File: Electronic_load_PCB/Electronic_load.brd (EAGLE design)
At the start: 121.9 x 88.6 mm, 111 parts, among them IC7 LM1117IMPX-5.0, J1 XT60-M, J2 B2B-XH, J3 B4B-XH, J4 B2B-XH, J5 B2B-XH, J6 B2B-XH, J7 B2B-XH, J8 B5B-XH, Q1 IRFP250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

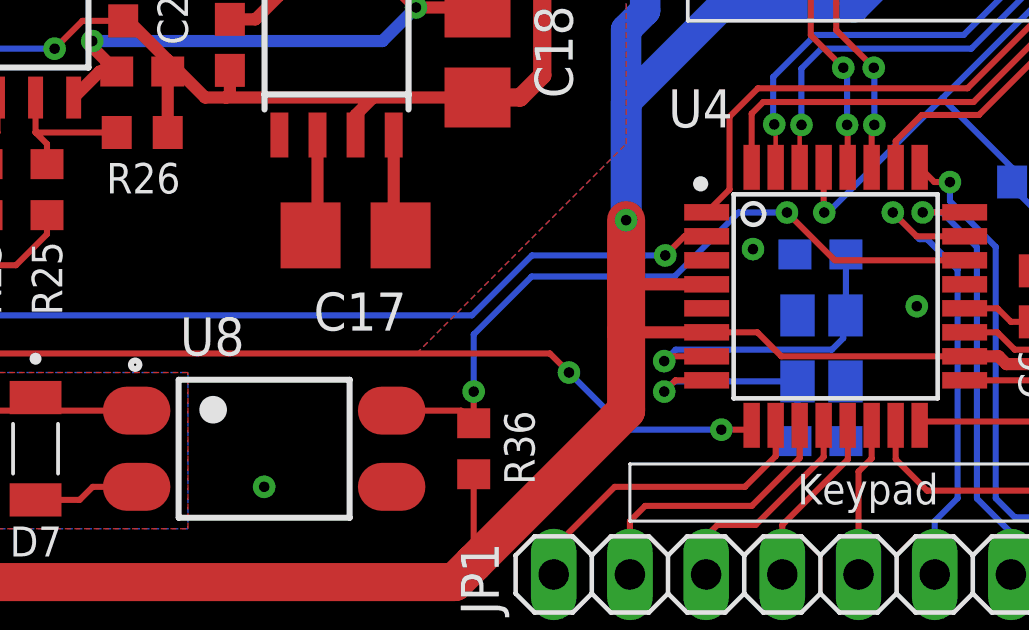
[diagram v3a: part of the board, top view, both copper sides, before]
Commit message: cleaned up schematic
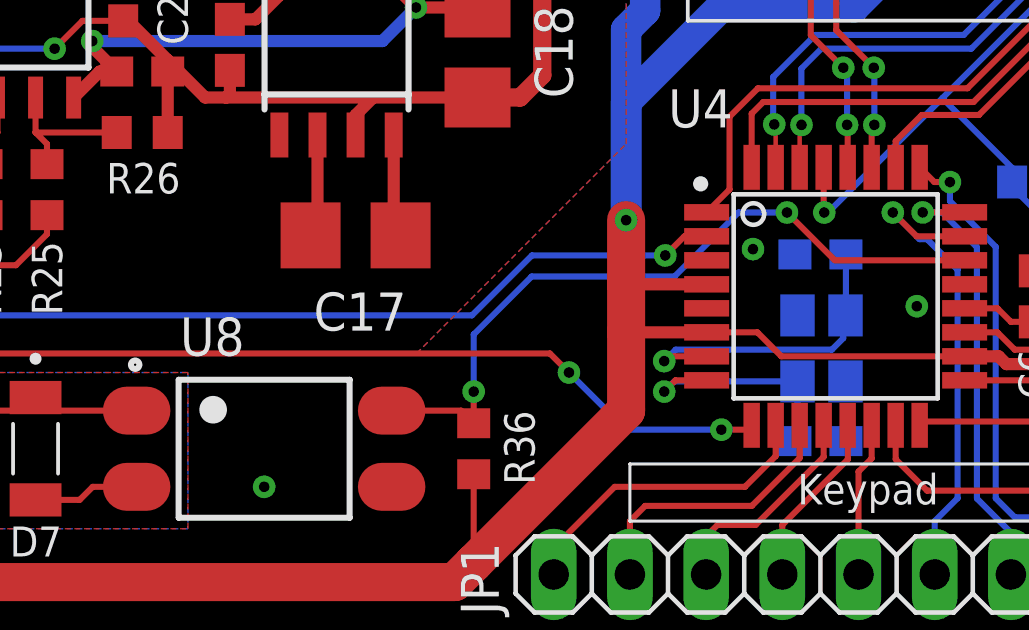
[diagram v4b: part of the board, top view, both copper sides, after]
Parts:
- C17, C18: value 100u -> 10u
- C19: value 100p -> omit
- C25: value 1u -> 100n
- R31: value 100R -> 1k
- R34: value 10k -> 1k
- R35: value 47k -> 10k
- renumbered Q12 to U$2
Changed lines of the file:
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@@
 <attribute name="VALUE" x="78.96788125" y="15.1125" size="2.083009375" layer="27" ratio="10" rot="SR0"/>
 </element>
-<element name="C17" library="rcl" library_urn="urn:adsk.eagle:library:334" package="CT3528" package3d_urn="urn:adsk.eagle:package:23325/2" value="100u" x="86.868" y="14.097" smashed="yes">
+<element name="C17" library="rcl" library_urn="urn:adsk.eagle:library:334" package="CT3528" package3d_urn="urn:adsk.eagle:package:23325/2" value="10u" x="86.868" y="14.097" smashed="yes">
 <attribute name="NAME" x="85.471" y="10.922" size="1.27" layer="25"/>
 <attribute name="POPULARITY" value="1" x="86.868" y="14.097" size="1.778" layer="27" display="off"/>
@@
 <attribute name="VALUE" x="84.328" y="10.922" size="1.27" layer="27"/>
 </element>
-<element name="C18" library="rcl" library_urn="urn:adsk.eagle:library:334" package="CT3528" package3d_urn="urn:adsk.eagle:package:23325/2" value="100u" x="90.932" y="20.193" smashed="yes" rot="R90">
+<element name="C18" library="rcl" library_urn="urn:adsk.eagle:library:334" package="CT3528" package3d_urn="urn:adsk.eagle:package:23325/2" value="10u" x="90.932" y="20.193" smashed="yes" rot="R90">
 <attribute name="NAME" x="94.107" y="18.669" size="1.27" layer="25" rot="R90"/>
 <attribute name="POPULARITY" value="1" x="90.932" y="20.193" size="1.778" layer="27" rot="R90" display="off"/>
@@
 <attribute name="VALUE" x="94.107" y="17.653" size="1.27" layer="27" rot="R90"/>
 </element>
-<element name="C19" library="rcl" library_urn="urn:adsk.eagle:library:334" package="C0603" package3d_urn="urn:adsk.eagle:package:23616/2" value="100p" x="84.963" y="25.273" smashed="yes">
+<element name="C19" library="rcl" library_urn="urn:adsk.eagle:library:334" package="C0603" package3d_urn="urn:adsk.eagle:package:23616/2" value="omit" x="84.963" y="25.273" smashed="yes">
 <attribute name="NAME" x="84.455" y="26.162" size="1.016" layer="25"/>
 <attribute name="POPULARITY" value="73" x="84.963" y="25.273" size="1.778" layer="27" display="off"/>
@@
 <attribute name="VALUE" x="60.325" y="33.655" size="1.27" layer="28" rot="MR180"/>
 </element>
-<element name="C25" library="rcl" library_urn="urn:adsk.eagle:library:334" package="C0603" package3d_urn="urn:adsk.eagle:package:23616/2" value="1u" x="82.677" y="20.447" smashed="yes" rot="R270">
+<element name="C25" library="rcl" library_urn="urn:adsk.eagle:library:334" package="C0603" package3d_urn="urn:adsk.eagle:package:23616/2" value="100n" x="82.677" y="20.447" smashed="yes" rot="R270">
 <attribute name="NAME" x="82.169" y="24.384" size="1.016" layer="25" rot="R270"/>
 <attribute name="POPULARITY" value="73" x="82.677" y="20.447" size="1.016" layer="27" rot="R270" display="off"/>
@@
 <attribute name="VALUE" x="32.385" y="17.78" size="1.27" layer="27" ratio="10"/>
 </element>
-<element name="R31" library="rcl" library_urn="urn:adsk.eagle:library:334" package="R0805" package3d_urn="urn:adsk.eagle:package:23553/2" value="100R" x="30.48" y="15.875" smashed="yes" rot="MR180">
+<element name="R31" library="rcl" library_urn="urn:adsk.eagle:library:334" package="R0805" package3d_urn="urn:adsk.eagle:package:23553/2" value="1k" x="30.48" y="15.875" smashed="yes" rot="MR180">
 <attribute name="NAME" x="29.337" y="17.907" size="1.016" layer="26" rot="MR180"/>
 <attribute name="POPULARITY" value="86" x="30.48" y="15.875" size="1.778" layer="28" rot="MR180" display="off"/>
@@
 </element>
 <element name="U$1" library="custom_heatsink" package="TO220_HEATSINK" override_package3d_urn="urn:adsk.eagle:package:36629292/4" override_package_urn="urn:adsk.eagle:footprint:36629293/2" value="TO220_HEATSINK" x="29.21" y="7.112" smashed="yes"/>
-<element name="R34" library="rcl" library_urn="urn:adsk.eagle:library:334" package="R0603" package3d_urn="urn:adsk.eagle:package:23555/3" value="10k" x="72.39" y="6.985" smashed="yes" rot="R270">
+<element name="R34" library="rcl" library_urn="urn:adsk.eagle:library:334" package="R0603" package3d_urn="urn:adsk.eagle:package:23555/3" value="1k" x="72.39" y="6.985" smashed="yes" rot="R270">
 <attribute name="NAME" x="73.406" y="8.255" size="1.016" layer="25" rot="R270"/>
 <attribute name="POPULARITY" value="70" x="72.39" y="6.985" size="1.778" layer="27" rot="R270" display="off"/>
@@
 <attribute name="VALUE" x="70.485" y="7.62" size="1.27" layer="27" rot="R270"/>
 </element>
-<element name="R35" library="rcl" library_urn="urn:adsk.eagle:library:334" package="R0603" package3d_urn="urn:adsk.eagle:package:23555/3" value="47k" x="113.03" y="15.875" smashed="yes" rot="MR90">
+<element name="R35" library="rcl" library_urn="urn:adsk.eagle:library:334" package="R0603" package3d_urn="urn:adsk.eagle:package:23555/3" value="10k" x="113.03" y="15.875" smashed="yes" rot="MR90">
 <attribute name="NAME" x="112.4966" y="17.4244" size="1.016" layer="26" rot="MR90"/>
 <attribute name="POPULARITY" value="70" x="113.03" y="15.875" size="1.778" layer="28" rot="MR90" display="off"/>
@@
 <attribute name="MF" value="Sharp Microelectronics" x="83.82" y="6.985" size="1.778" layer="27" display="off"/>
 <attribute name="MP" value="PC817X2NIP0F" x="83.82" y="6.985" size="1.778" layer="27" display="off"/>
+<attribute name="NAME" x="81.014759375" y="10.0908" size="1.27238125" layer="25"/>
 <attribute name="NAME" x="81.01816875" y="10.08701875" size="1.27083125" layer="25"/>
-<attribute name="NAME" x="81.014759375" y="10.0908" size="1.27238125" layer="25"/>
 <attribute name="PACKAGE" value="SMD-4 Sharp" x="83.82" y="6.985" size="1.778" layer="27" display="off"/>
 <attribute name="PRICE" value="None" x="83.82" y="6.985" size="1.778" layer="27" display="off"/>
@@
 <attribute name="VALUE" x="101.727" y="9.144" size="1.27" layer="28" rot="MR180"/>
 </element>
-<element name="Q12" library="CRYSTAL_SMD_3,4x2.7mm" package="CRYSTAL_3,4X2,7" override_package3d_urn="urn:adsk.eagle:package:35472672/2" override_package_urn="urn:adsk.eagle:footprint:35472688/1" value="CRYSTAL_3,4X2,7" x="101.6" y="11.43" smashed="yes" rot="MR270"/>
 <element name="JP2" library="jst connectors" package="JST_B4B-XH-A(LF)(SN)" package3d_urn="urn:adsk.eagle:package:36544612/2" value="B4B-XH" x="114.935" y="45.085" smashed="yes" rot="R90">
 <attribute name="AVAILABILITY" value="In Stock" x="114.935" y="45.085" size="1.778" layer="27" rot="R90" display="off"/>
@@
 <attribute name="VALUE" x="92.202" y="-0.381" size="1.27" layer="27"/>
 </element>
+<element name="U$2" library="CRYSTAL_SMD_3,4x2.7mm" package="CRYSTAL_3,4X2,7" value="CRYSTAL_3,4X2,7" x="101.6" y="11.43" smashed="yes" rot="MR270"/>
 </elements>
 <signals>
@@
 <contactref element="C28" pad="2"/>
 <contactref element="C29" pad="2"/>
-<contactref element="Q12" pad="GND"/>
-<contactref element="Q12" pad="GND2"/>
 <contactref element="JP2" pad="4"/>
 <via x="51.8668" y="18.1356" extent="1-16" drill="0.35"/>
@@
 <wire x1="81.365975" y1="39.157025" x2="82.423" y2="38.1" width="0.6096" layer="16"/>
 <via x="88.773" y="35.433" extent="1-16" drill="0.35"/>
+<contactref element="U$2" pad="GND"/>
+<contactref element="U$2" pad="GND2"/>
 </signal>
 <signal name="DAC_OUT">
@@
 <signal name="XTL1">
 <contactref element="U4" pad="7"/>
-<contactref element="Q12" pad="CRST1"/>
 <contactref element="C28" pad="1"/>
-<wire x1="103.212" y1="13.462" x2="103.212" y2="11.442" width="0.2032" layer="16"/>
-<wire x1="103.212" y1="11.442" x2="103.2" y2="11.43" width="0.2032" layer="16"/>
-<wire x1="103.2" y1="11.43" x2="103.124" y2="11.354" width="0.2032" layer="16"/>
+<wire x1="103.212" y1="11.442" x2="103.212" y2="13.462" width="0.2032" layer="16"/>
 <wire x1="103.124" y1="11.354" x2="103.124" y2="10.668" width="0.2032" layer="16"/>
 <wire x1="103.124" y1="10.668" x2="102.743" y2="10.287" width="0.2032" layer="16"/>
@@
 <wire x1="97.314" y1="10.065" x2="98.57" y2="10.065" width="0.2032" layer="1"/>
 <wire x1="102.743" y1="10.287" x2="97.536" y2="10.287" width="0.2032" layer="16"/>
+<contactref element="U$2" pad="CRST1"/>
+<wire x1="103.2" y1="11.43" x2="103.124" y2="11.354" width="0.2032" layer="16"/>
+<wire x1="103.2" y1="11.43" x2="103.212" y2="11.442" width="0.2032" layer="16"/>
 </signal>
 <signal name="XTL2">
 <contactref element="U4" pad="8"/>
 <contactref element="C29" pad="1"/>
-<contactref element="Q12" pad="CRST2"/>
-<wire x1="101.6" y1="9.23" x2="101.6" y2="7.327" width="0.2032" layer="16"/>
 <wire x1="101.6" y1="7.327" x2="101.512" y2="7.239" width="0.2032" layer="16"/>
-<wire x1="101.6" y1="9.23" x2="97.495" y2="9.23" width="0.2032" layer="16"/>
 <wire x1="97.495" y1="9.23" x2="97.155" y2="8.89" width="0.2032" layer="16"/>
 <via x="97.155" y="8.89" extent="1-16" drill="0.35"/>
 <wire x1="97.155" y1="8.89" x2="97.53" y2="9.265" width="0.2032" layer="1"/>
 <wire x1="97.53" y1="9.265" x2="98.57" y2="9.265" width="0.2032" layer="1"/>
+<contactref element="U$2" pad="CRST2"/>
+<wire x1="101.6" y1="9.23" x2="97.495" y2="9.23" width="0.2032" layer="16"/>
+<wire x1="101.6" y1="9.23" x2="101.6" y2="7.327" width="0.2032" layer="16"/>
 </signal>
 <signal name="KP1">
